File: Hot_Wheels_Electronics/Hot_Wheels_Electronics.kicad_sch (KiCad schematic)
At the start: 30 parts, among them J1 motor_output_a, J2 motor_output_b, J3 Conn_01x05_Socket, M1 motor_driver: DRV8833PW, SW1 main_switch, U1 esp32-wemos-d1-mini, U2 ESP32-WROOM-32, U3 BMI160, U4 MiniBuck_3A, U5 MiniBuck_3A, U6 ADS1115IDGS

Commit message: added battery voltage sense circuit
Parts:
- added C10: 100 nF, Capacitor_SMD:C_1206_3216Metric_Pad1.33x1.80mm_HandSolder, symbol Device:C
- added R10: 33 k, Resistor_SMD:R_1206_3216Metric_Pad1.30x1.75mm_HandSolder, symbol Device:R
- added R9: 100 k, Resistor_SMD:R_1206_3216Metric_Pad1.30x1.75mm_HandSolder, symbol Device:R
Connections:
- net +BATT: now also R9.1
- net GND: now also C10.2, R10.2
- net battery_voltage_sense: now also C10.1, R10.1, R9.2
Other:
- moved on the sheet: BT1, C1, C2, C3, C4, C6, C7, J1, J2, M1, R1, R3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

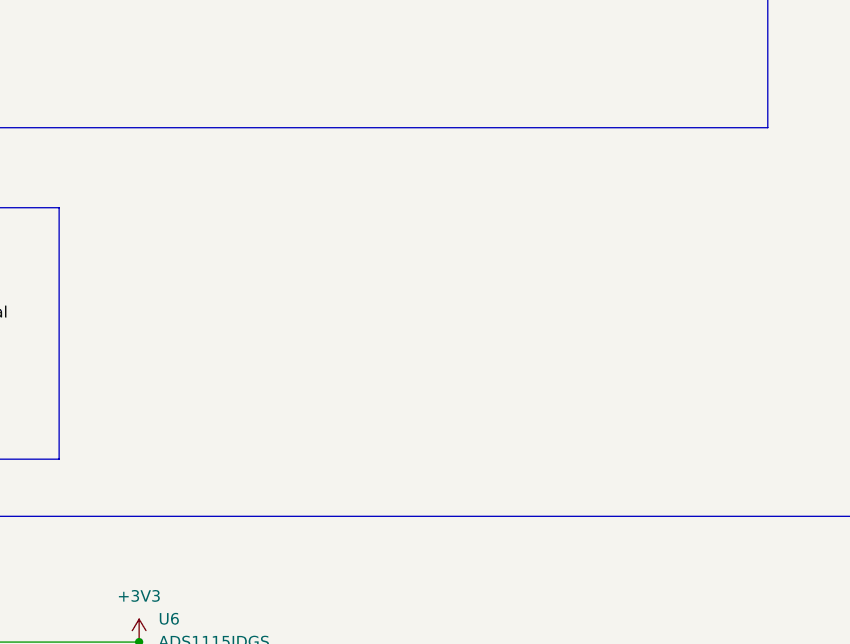
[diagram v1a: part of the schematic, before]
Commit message: add motor temperature sensing
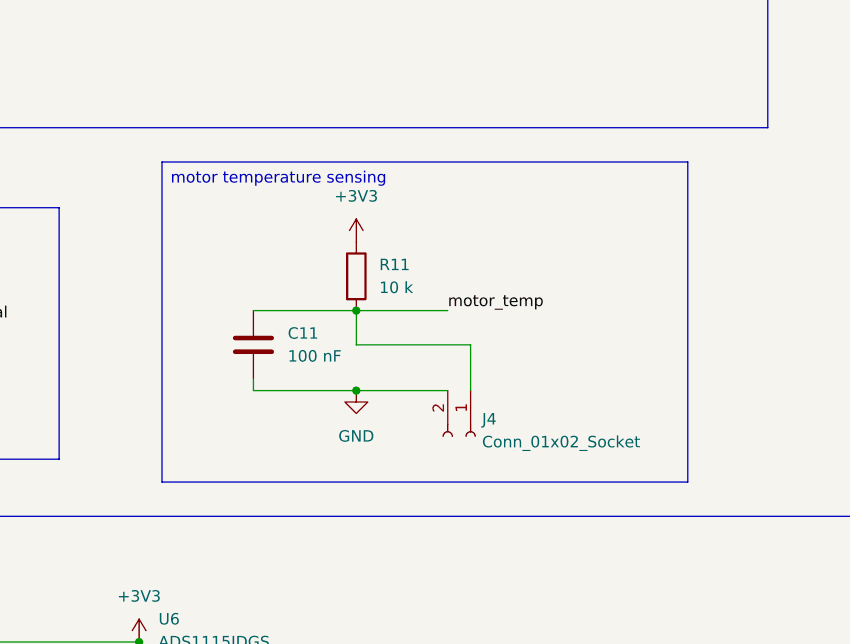
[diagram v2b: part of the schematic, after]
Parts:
- added C11: 100 nF, Capacitor_SMD:C_1206_3216Metric_Pad1.33x1.80mm_HandSolder, symbol Device:C
- added J4: Conn_01x02_Socket, Connector_JST:JST_ZH_B2B-ZR-SM4-TF_1x02-1MP_P1.50mm_Vertical, symbol Connector:Conn_01x02_Socket
- added R11: 10 k, Resistor_SMD:R_1206_3216Metric_Pad1.30x1.75mm_HandSolder, symbol Device:R
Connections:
- net +3V3: now also R11.1
- net GND: now also C11.2, J4.2 (Pin_2)
- net motor_temp: now also C11.1, J4.1 (Pin_1), R11.2

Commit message: add wheel speed sensor interface
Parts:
- added J5: Conn_01x03_Socket, Connector_JST:JST_ZH_B3B-ZR-SM4-TF_1x03-1MP_P1.50mm_Vertical, symbol Connector:Conn_01x03_Socket
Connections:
- net +3V3: now also J5.1 (Pin_1)
- net GND: now also J5.3 (Pin_3)
- net wheel_speed: now also J5.2 (Pin_2)

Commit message: add forward tof sensor interface
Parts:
- added J6: Conn_01x06_Socket, Connector_JST:JST_PH_B6B-PH-SM4-TB_1x06-1MP_P2.00mm_Vertical, symbol Connector:Conn_01x06_Socket
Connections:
- net +3V3: now also J6.1 (Pin_1)
- net GND: now also J6.2 (Pin_2)
- net i2c_scl: now also J6.4 (Pin_4)
- net i2c_sda: now also J6.3 (Pin_3)
- net tof_int: now reaches U2.26 (IO4)
- net tof_int: now also J6.5 (Pin_5)
- net tof_xshut: now reaches U2.29 (IO5)
- net tof_xshut: now also J6.6 (Pin_6)
- no-connect marks 16 -> 14

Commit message: add floor colour sensor interface
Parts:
- added J7: Conn_01x04_Socket, Connector_JST:JST_PH_B4B-PH-SM4-TB_1x04-1MP_P2.00mm_Vertical, symbol Connector:Conn_01x04_Socket
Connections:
- net +3V3: now also J7.1 (Pin_1)
- net GND: now also J7.2 (Pin_2)
- net i2c_scl: now also J7.3 (Pin_3)
- net i2c_sda: now also J7.4 (Pin_4)

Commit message: assign compact but beefier footprint for power switch
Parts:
- SW1: footprint (none) -> Connector_PinHeader_2.54mm:PinHeader_1x02_P2.54mm_Vertical_SMD_Pin1Left
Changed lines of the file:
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@@
 			)
 		)
-		(property "Footprint" ""
+		(property "Footprint" "Connector_PinHeader_2.54mm:PinHeader_1x02_P2.54mm_Vertical_SMD_Pin1Left"
 			(at 44.45 35.56 0)
 			(hide yes)

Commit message: add external brushless esc interface
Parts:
- added J8: Conn_01x02_Socket, Connector_JST:JST_ZH_B2B-ZR-SM4-TF_1x02-1MP_P1.50mm_Vertical, symbol Connector:Conn_01x02_Socket
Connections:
- net GND: now also J8.2 (Pin_2)
- net esc_signal: now reaches U2.23 (IO15)
- net esc_signal: now also J8.1 (Pin_1)
- no-connect marks 14 -> 13
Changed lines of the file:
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@@
 		)
 	)
+	(text_box "ESC output"
+		(exclude_from_sim no)
+		(at 25.4 247.65 0)
+		(size 41.91 20.32)
+		(margins 0.9525 0.9525 0.9525 0.9525)
+		(stroke
+			(width 0)
+			(type solid)
+		)
+		(fill
+			(type none)
+		)
+		(effects
+			(font
+				(size 1.27 1.27)
+			)
+			(justify left top)
+		)
+	)
 	(text_box "servo"
 		(exclude_from_sim no)
@@
 	)
 	(no_connect
-		(at 267.97 102.87)
-	)
-	(no_connect
 		(at 267.97 135.89)
 	)
@@
 	(wire
 		(pts
+			(xy 267.97 102.87) (xy 271.78 102.87)
+		)
+		(stroke
+			(width 0)
+			(type default)
+		)
+	)
+	(wire
+		(pts
 			(xy 340.36 229.87) (xy 360.68 229.87)
 		)
@@
 		)
 	)
+	(label "esc_signal"
+		(at 271.78 102.87 0)
+		(effects
+			(font
+				(size 1.27 1.27)
+			)
+			(justify left bottom)
+		)
+	)
 	(label "i2c_sda"
 		(at 158.75 43.18 0)
@@
 		)
 	)
+	(label "esc_signal"
+		(at 39.37 255.27 180)
+		(effects
+			(font
+				(size 1.27 1.27)
+			)
+			(justify right bottom)
+		)
+	)
 	(label "tof_xshut"
 		(at 271.78 92.71 0)
@@
 	(symbol
 		(lib_id "power:GND")
+		(at 39.37 257.81 0)
+		(unit 1)
+		(body_style 1)
+		(exclude_from_sim no)
+		(in_bom yes)
+		(on_board yes)
+		(in_pos_files yes)
+		(dnp no)
+		(fields_autoplaced yes)
+		(property "Reference" "#PWR041"
+			(at 39.37 264.16 0)
+			(hide yes)
+			(show_name no)
+			(do_not_autoplace no)
+			(effects
+				(font
+					(size 1.27 1.27)
+				)
+			)
+		)
+		(property "Value" "GND"
+			(at 39.37 262.89 0)
+			(show_name no)
+			(do_not_autoplace no)
+			(effects
+				(font
+					(size 1.27 1.27)
+				)
+			)
+		)
+		(property "Footprint" ""
+			(at 39.37 257.81 0)
+			(hide yes)
+			(show_name no)
+			(do_not_autoplace no)
+			(effects
+				(font
+					(size 1.27 1.27)
+				)
+			)
+		)
+		(property "Datasheet" ""
+			(at 39.37 257.81 0)
+			(hide yes)
+			(show_name no)
+			(do_not_autoplace no)
+			(effects
+				(font
+					(size 1.27 1.27)
+				)
+			)
+		)
+		(property "Description" "Power symbol creates a global label with name \"GND\" , ground"
+			(at 39.37 257.81 0)
+			(hide yes)
+			(show_name no)
+			(do_not_autoplace no)
+			(effects
+				(font
+					(size 1.27 1.27)
+				)
+			)
+		)
+		(pin "1"
+		)
+		(instances
+			(project "Hot_Wheels_Electronics"
+				(path "/753fef37-370a-4893-8adb-358cd7fc1669"
+					(reference "#PWR041")
+					(unit 1)
+				)
+			)
+		)
+	)
+	(symbol
+		(lib_id "power:GND")
 		(at 393.7 189.23 0)
 		(unit 1)
@@
 	)
 	(symbol
+		(lib_id "Connector:Conn_01x02_Socket")
+		(at 44.45 255.27 0)
+		(unit 1)
+		(body_style 1)
+		(exclude_from_sim no)
+		(in_bom yes)
+		(on_board yes)
+		(in_pos_files yes)
+		(dnp no)
+		(fields_autoplaced yes)
+		(property "Reference" "J8"
+			(at 45.72 255.2699 0)
+			(show_name no)
+			(do_not_autoplace no)
+			(effects
+				(font
+					(size 1.27 1.27)
+				)
+				(justify left)
+			)
+		)
+		(property "Value" "Conn_01x02_Socket"
+			(at 45.72 257.8099 0)
+			(show_name no)
+			(do_not_autoplace no)
+			(effects
+				(font
+					(size 1.27 1.27)
+				)
+				(justify left)
+			)
+		)
+		(property "Footprint" "Connector_JST:JST_ZH_B2B-ZR-SM4-TF_1x02-1MP_P1.50mm_Vertical"
+			(at 44.45 255.27 0)
+			(hide yes)
+			(show_name no)
+			(do_not_autoplace no)
+			(effects
+				(font
+					(size 1.27 1.27)
+				)
+			)
+		)
+		(property "Datasheet" ""
+			(at 44.45 255.27 0)
+			(hide yes)
+			(show_name no)
+			(do_not_autoplace no)
+			(effects
+				(font
+					(size 1.27 1.27)
+				)
+			)
+		)
+		(property "Description" "Generic connector, single row, 01x02, script generated"
+			(at 44.45 255.27 0)
+			(hide yes)
+			(show_name no)
+			(do_not_autoplace no)
+			(effects
+				(font
+					(size 1.27 1.27)
+				)
+			)
+		)
+		(pin "2"
+		)
+		(pin "1"
+		)
+		(instances
+			(project "Hot_Wheels_Electronics"
+				(path "/753fef37-370a-4893-8adb-358cd7fc1669"
+					(reference "J8")
+					(unit 1)
+				)
+			)
+		)
+	)
+	(symbol
 		(lib_id "Connector:Conn_01x06_Socket")
 		(at 173.99 82.55 0)
@@
 	)
 	(group ""
+		(members "13a5c097-c5b0-4a1c-b233-7bf1c338f96f" "2d06d671-f1fb-4f6b-a585-8ddd0b6227c0"
+			"3e731b21-44dc-4648-9aca-b1507ab0f056" "cd6089f3-a7ae-42bd-9338-69cd3409e9a4"
+		)
+	)
+	(group ""

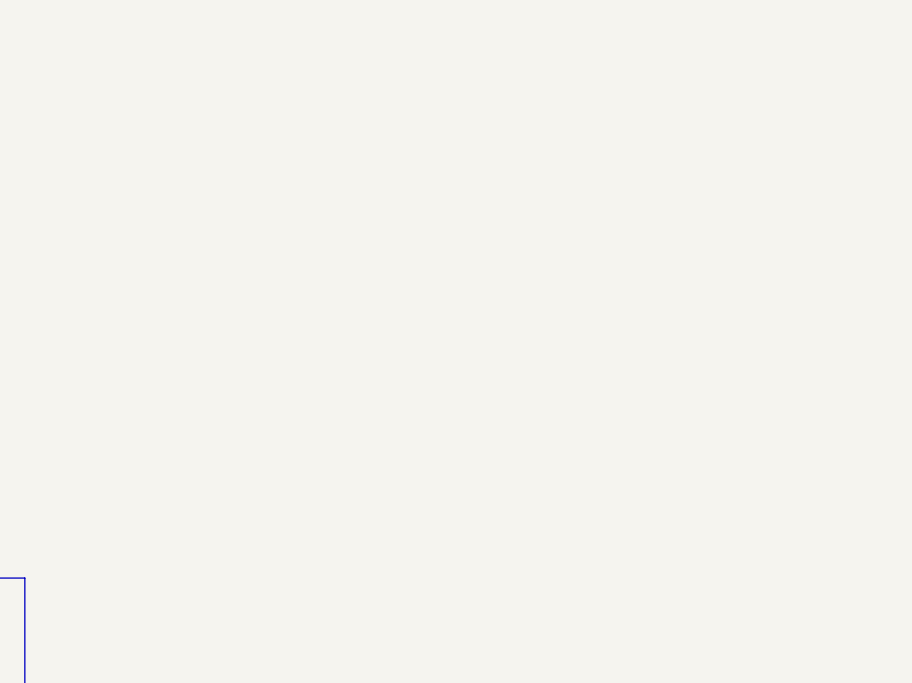
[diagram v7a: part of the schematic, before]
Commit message: add ESP32 local supply decoupling
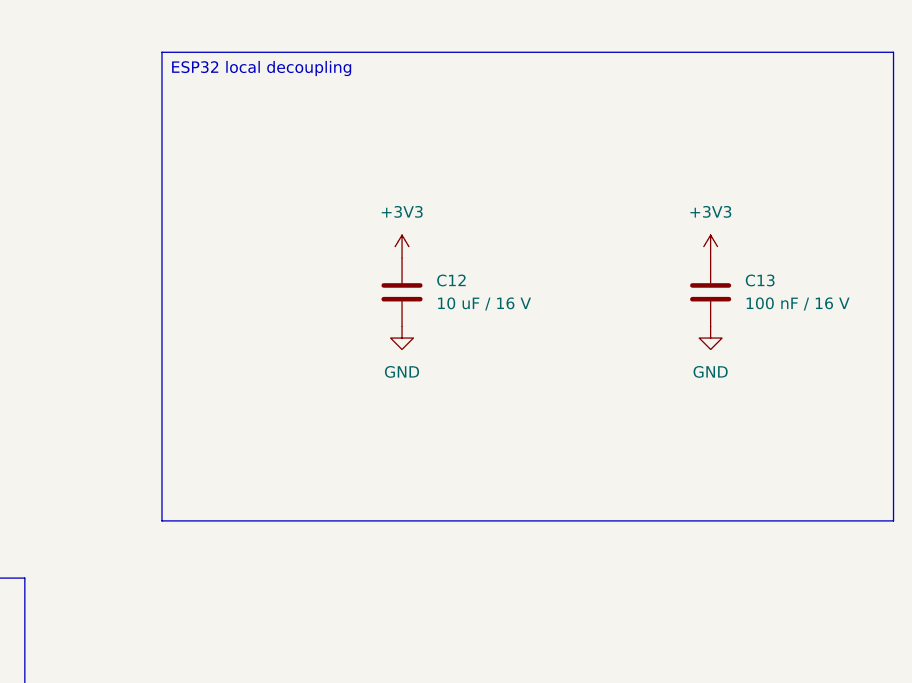
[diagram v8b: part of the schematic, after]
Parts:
- added C12: 10 uF / 16 V, Capacitor_SMD:C_1206_3216Metric_Pad1.33x1.80mm_HandSolder, symbol Device:C
- added C13: 100 nF / 16 V, Capacitor_SMD:C_1206_3216Metric_Pad1.33x1.80mm_HandSolder, symbol Device:C
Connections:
- net +3V3: now also C12.1, C13.1
- net GND: now also C12.2, C13.2
